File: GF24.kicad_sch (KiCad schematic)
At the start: 65 parts, among them J1 Conn_ARM_SWD_TagConnect_TC2030, J2 USB4110GFA, J3 S2B-PH-SM4-TB, J4 0533980671, J5 0533980671, Q1 3904, Q2 DMN3731U-7, Q3 DMN3731U-7, SW2 BOOT, U1 STM32F031C4T6, U2 SAM-M10Q, U3 TPS745, U4 LTC1733, U5 NE555D, U6 M24C02-WMN6TP, Y1 CS06465-32M

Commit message: updating regulator
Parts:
- removed C14: 0.1uF, MB-Generic:C0603_medium, symbol Device:C
- removed D4: LED, symbol Device:LED
- removed R10: 10k, MB-Generic:R0603_medium, symbol Device:R
- removed R11, R12: 4.7k, MB-Generic:R0603_medium, symbol Device:R
- removed R9: 1k, MB-Generic:R0603_medium, symbol Device:R
- removed U3: TPS745, MB-DFN:6-WDFN, symbol MB-V-REG:TPS74533PQWDRVRQ1
- removed U6: M24C02-WMN6TP, MB-SOIC:SO-8_STM, symbol MB-EEPROM:M24C02-WMN6TP
- added U6: STM32F102C8Tx, Package_QFP:LQFP-48_7x7mm_P0.5mm, symbol MCU_ST_STM32F1:STM32F102C8Tx
- added U7: ~, Package_TO_SOT_SMD:SOT-223-6, symbol MB-V-REG:TPS79533DCQR
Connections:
- net +3V3: now also U7.4 (OUT)
- net REG_I: now also U7.1 (EN)
- net EEPROM-N-WC: no longer names the net of U1.20 (PB2)
- net I2C-SCL: no longer names the net of U1.21 (PB10)
- net I2C-SDA: no longer names the net of U1.22 (PB11)
- new net: U6.23 (VSS), U6.35 (VSS), U6.47 (VSS)
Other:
- note added: "swap for TPS79533DCQR"
- note removed: "EEPROM"
- note removed: "stay under 10mA"
- moved on the sheet: C11, C12, C13, C16, C7, D2, D3, D6, R19, R21, R22, R5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

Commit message: soft complete Rev 2 schematic
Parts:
- removed C1, C2: 4.7uF, MB-Generic:C1206_medium, symbol Device:C
- removed C4: 0.1uF, MB-Generic:C0603_medium, symbol Device:C
- removed C5, C6: 10pF, MB-Generic:C0402_medium, symbol Device:C
- removed J1: Conn_ARM_SWD_TagConnect_TC2030, MB-Conn:Tag-Connect_TC2030-IDC-FP_2x03_P1.27mm_Vertical, symbol Connector:Conn_ARM_SWD_TagConnect_TC2030
- removed J3: S2B-PH-SM4-TB, MB-Conn:JST_S2B-PH-SM4-TB, symbol MB-Conn:S2B-PH-SM4-TB
- removed J4, J5: 0533980671, MB-Conn:MOLEX_0533980671, symbol MB-Conn:0533980671
- removed R1: 10k, MB-Generic:R0603_medium, symbol Device:R
- removed R19, R21, R7, R8: 1k, MB-Generic:R0603_medium, symbol Device:R
- removed R22: 330k, MB-Generic:R0603_medium, symbol Device:R
- removed SW1: ~, MB-SW:PTS815SJM250SMTRLFS, symbol MB-SW:PTS815SJM250SMTRLFS
- removed SW2: BOOT, MB-SW:CJS-1200TA, symbol Switch:SW_Nidec_CAS-120A1
- removed SW3: ~, MB-SW:TL1016AAF160QG, symbol MB-SW:TL1016AAF160QG
- removed U1: STM32F031C4T6, MB-STM:LQFP-48_7x7mm_P0.5mm, symbol MCU_ST_STM32F0:STM32F031C4Tx
- removed U5: NE555D, symbol Timer:NE555D
- removed Y1: CS06465-32M, MB-Crystal:CS06465-32M, symbol Device:Crystal_GND24
- added C10, C12, C13, C15, C19, C8: 100nf, MB-Generic:C1206_medium, symbol Device:C
- added C11, C9: 10uF, MB-Generic:C1206_medium, symbol Device:C
- added C14: 1uF, MB-Generic:C1206_medium, symbol Device:C
- added D1, D4, D8, D9: LED, symbol Device:LED
- added J2: S2B-PH-SM4-TB, MB-Conn:JST_S2B-PH-SM4-TB, symbol MB-Conn:S2B-PH-SM4-TB
- added J3, J6: Conn_01x06_Pin, symbol Connector:Conn_01x06_Pin
- added J4: Conn_ARM_SWD_TagConnect_TC2030, Connector:Tag-Connect_TC2030-IDC-FP_2x03_P1.27mm_Vertical, symbol Connector:Conn_ARM_SWD_TagConnect_TC2030
- added J5: Conn_01x04_Pin, symbol Connector:Conn_01x04_Pin
- added R12: 10k, MB-Generic:R0603_medium, symbol Device:R
- added R2, R3: ~, MB-Generic:R0603_medium, symbol Device:R
- added R4, R5, R6: 1k, MB-Generic:R0603_medium, symbol Device:R
- added S1: 1-1825027-1, MB-SW:SW_1-1825027-1, symbol MB-SW:1-1825027-1
- added SW2: ~, MB-SW:PTS815SJM250SMTRLFS, symbol MB-SW:PTS815SJM250SMTRLFS
- added SW4: BOOT, Button_Switch_SMD:Nidec_Copal_CAS-120A, symbol Switch:SW_Nidec_CAS-120A1
- added TP1, TP2, TP3, TP4, TP5, TP6: TestPoint, symbol Connector:TestPoint
- added X1: ECS-2520MV-160-CN, Oscillator:Oscillator_SMD_ECS_2520MV-xxx-xx-4Pin_2.5x2.0mm, symbol Oscillator:ECS-2520MV-xxx-xx
- C16: value 2.2uF -> 100nf; Distributor Link (none) -> https://www.digikey.com/en/products/detail/kemet/C1206C475K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; Manufacturer (none) -> KEMET; Manufacturer PN (none) -> C1206C475K8RACTU
- C7: value 10nF -> 10uF; footprint MB-Generic:C0402_medium -> MB-Generic:C1206_medium; Distributor Link https://www.digikey.com/en/products/detail/kemet/c0402c103k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 -> https://www.digikey.com/en/products/detail/kemet/C1206C475K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; Manufacturer PN C0402C103K8RACTU -> C1206C475K8RACTU
- Q1: footprint MB-SOT:SOT-23-3 -> Package_TO_SOT_SMD:SOT-323_SC-70
- R8: renamed from R14; value 1k -> was 1k
- R9: renamed from R3; value 1k -> was 1k
- U1: renamed from U7; value ~ -> TPS79533DCQR
- renumbered C9 to C1, C10 to C17, C15 to C18, C8 to C2, C11 to C4, C12 to C5, C13 to C6, D6 to D5, D5 to D6, D1 to D7, J2 to J1, Q3 to Q2, Q2 to Q3, R6 to R1, R4 to R10, R13 to R11, R2 to R13, R15 to R14, R16 to R15, R18 to R16, R5 to R7, SW4 to SW1, SW5 to SW3, U4 to U2, U2 to U3, U6 to U4
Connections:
- net VBUS is gone; now on an unnamed net: C4.1, J1.A4/B9 (VBUS), J1.B4/A9 (VBUS), R1.2, U2.2 (VCC), U2.8 (SEL)
- net +3V3: now also C7.1, U4.1 (VBAT), U4.24 (VDD), U4.36 (VDD), U4.48 (VDD), U4.9 (VDDA), C10.1, C11.1, C12.1, C13.1, C14.1, C15.1, C19.1, C8.1, C9.1, D1.2 (A), D8.2 (A), D9.2 (A), J4.1 (VCC), J5.1 (Pin_1), J6.6 (Pin_6), SW4.1 (C), TP1.1, X1.4 (VDD); no longer C3.1, R8.2, R9.2
- net ACT-H: now also S1.1
- net BAT+: no longer C6.1, U2.9 (BAT)
- net BOOT0_RES: now also R12.1, SW4.2 (B)
- net BUTTON: now also U4.42 (PB6)
- net BUZZER: now also U4.39 (PB3)
- net GND: now also C16.2, Q2.3 (S), Q3.3 (S), U1.3 (GND), U1.6 (GND), U4.23 (VSS), U4.35 (VSS), U4.47 (VSS), U4.8 (VSSA), C10.2, C11.2, C12.2, C13.2, C14.2, C15.2, C19.2, C8.2, C9.2, J2.1, J4.5 (GND), J5.4 (Pin_4), J6.1 (Pin_1), R2.2, S1.2, SW2.2, SW4.3 (A), TP2.1, X1.2 (GND); no longer C16.1, Q2.2 (S), Q3.2 (S)
- net GNSS-3V3: now also D2.2 (A), J3.6 (Pin_6)
- net GNSS-GND: now also J3.1 (Pin_1), R3.2
- net GNSS-N-RESET: now also J3.5 (Pin_5)
- net GNSS-RX: now also J3.4 (Pin_4)
- net GNSS-ST-N-RESET: now also U4.11 (PA1), J6.5 (Pin_5)
- net GNSS-ST-TIMEPULSE: now also U4.14 (PA4), J6.2 (Pin_2)
- net GNSS-TIMEPULSE: now also J3.2 (Pin_2)
- net GNSS-TX: now also J3.3 (Pin_3)
- net MODE: now also U4.43 (PB7)
- net NACPR: now also R4.2; no longer D2.1 (K)
- net NCHRG: now also R6.2; no longer D5.1 (K)
- net NFAULT: now also R5.2; no longer D3.1 (K)
- net NRST: now also C16.1, U4.7 (NRST), J4.3 (~{RESET}), SW2.4
- net REG_I: now also U1.2 (IN)
- net STATG: now also U4.41 (PB5)
- net STATG_QG: now also Q3.2 (G); no longer Q3.1 (G)
- net STATG_QI: now also Q3.1 (D); no longer Q3.3 (D)
- net STATR: now also U4.40 (PB4)
- net STATR_QG: now also Q2.2 (G); no longer Q2.1 (G)
- net STATR_QI: now also Q2.1 (D); no longer Q2.3 (D)
- net SWDCLK: now also U4.37 (PA14), J4.4 (SWCLK)
- net SWDIO: now also U4.34 (PA13), J4.2 (SWDIO)
- net at D3.2 (A): now also D5.2 (A), D4.2 (A), TP5.1
- net at U1.5 (NR): now also C3.1
- net GNSS-ST-TX2: now reaches U4.12 (PA2)
- net GNSS-ST-TX2: now also J6.4 (Pin_4), TP3.1
- net GNSS-ST-RX2: now reaches U4.13 (PA3)
- net GNSS-ST-RX2: now also J6.3 (Pin_3), TP4.1
- net DEBUG_ST_TX: now reaches U4.21 (PB10)
- net DEBUG_ST_TX: now also J5.2 (Pin_2)
- net DEBUG_ST_RX: now reaches U4.22 (PB11)
- net DEBUG_ST_RX: now also J5.3 (Pin_3)
- net BACKUP_DEBUG_ST_TX: now reaches U4.30 (PA9)
- net BACKUP_DEBUG_ST_RX: now reaches U4.31 (PA10)
- net at U4.44 (BOOT0): now also R12.2
- net at U4.5 (PD0): now also X1.3 (OUT)
- new net: D2.1 (K), R3.1
- new net: C6.1, J2.2, TP6.1, U2.9 (BAT)
- new net: D8.1 (K), R8.2
- new net: D3.1 (K), R4.1
- new net: D9.1 (K), R9.2
- new net: D1.1 (K), R2.1
- new net: D5.1 (K), R6.1
- new net: D4.1 (K), R5.1
- no-connect marks 43 -> 42
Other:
- note added: "HSE Bypass"
- note added: "INPUTS/OUTPUTS"
- note added: "No more than 5V should ever be applied to this IC (AMR 7V)"
- note added: "UART Debug"
- note added: "VBAT"
- note added: "external"
- note added: "right angle"
- note removed: "CHARGING"
- note removed: "CONTROLLER"
- note removed: "High Speed External Crystal"
- note removed: "INPUTS"
- note removed: "No more than 5V should ever be applied to this circuit (VBUS-GND)"
- note removed: "OUTPUTS"
- note removed: "PG is open drain when power is not good (lmao). can handle 10mA"
- note removed: "SUBCOMPONENTS"
- note removed: "lmao"
- note removed: "messy :("
- note removed: "swap for TPS79533DCQR"
- note removed: "uC"
- note removed: "uC Power Stability"
- moved on the sheet: BZ1, C1, C17, C18, C2, C4, C5, C6, D5, D6, D7, J1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

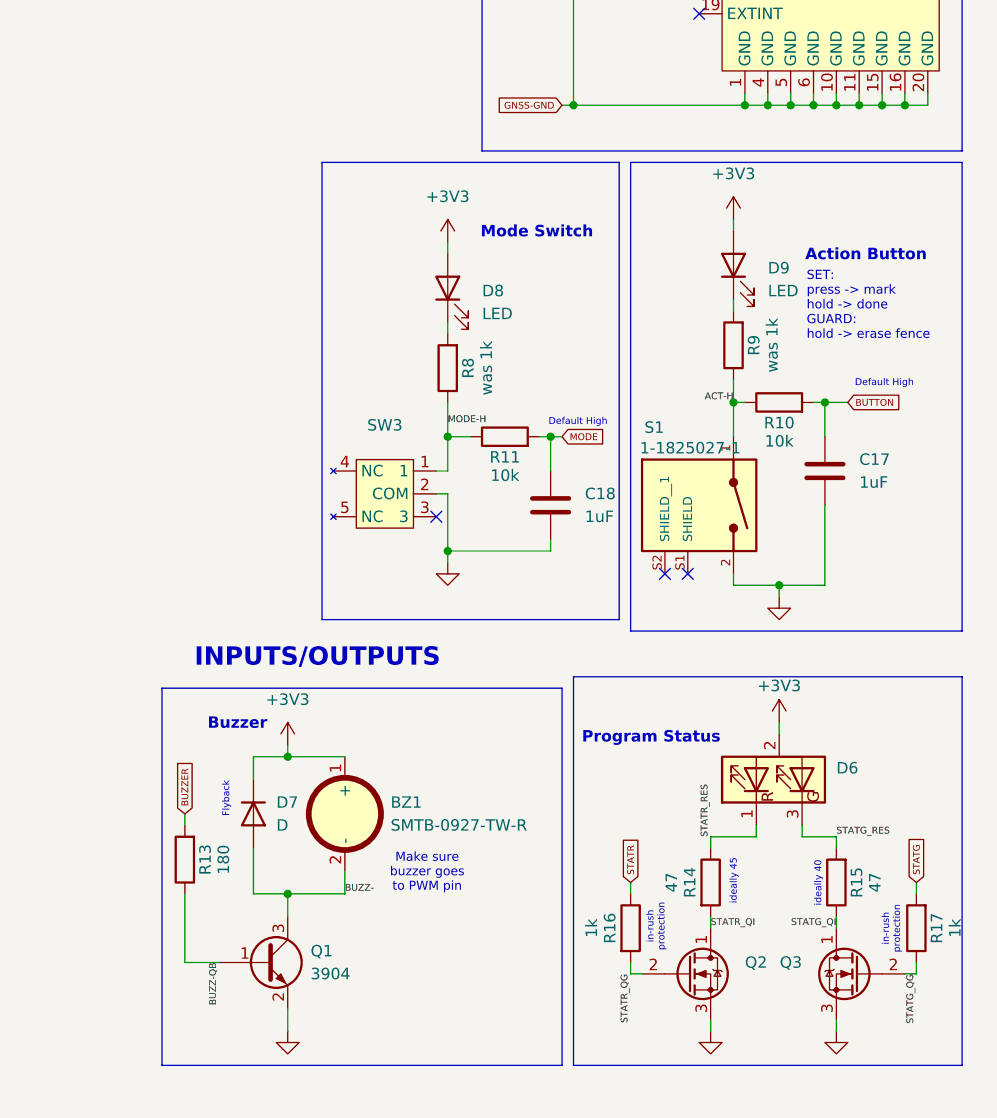
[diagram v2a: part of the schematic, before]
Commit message: changed status LEDs based on testing
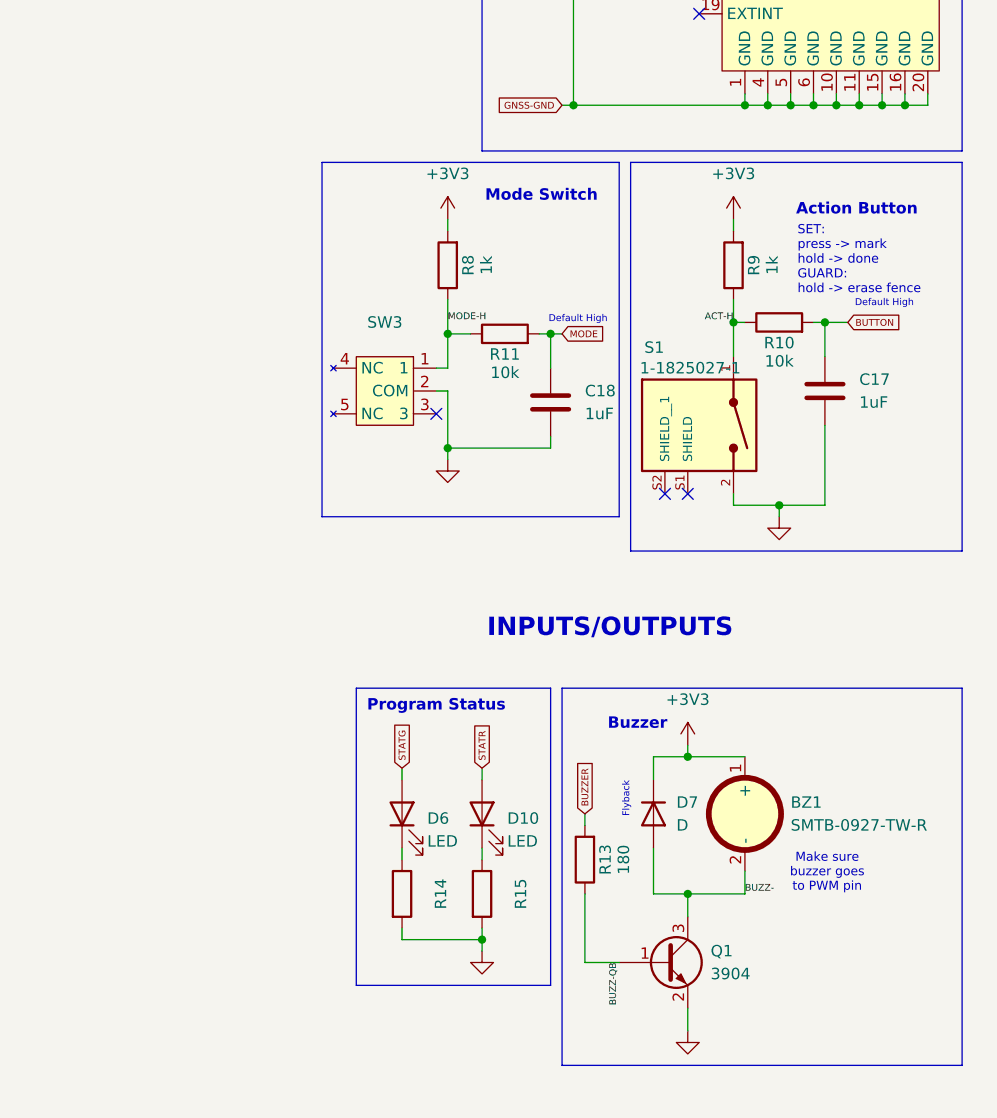
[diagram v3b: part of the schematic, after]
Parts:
- removed D6: APBDA3020SURKCGKC-GX, MB-Opto:Kingbright-APBDA3020, symbol MB-Opto:APBDA3020SURKCGKC-GX
- removed D8, D9: LED, symbol Device:LED
- removed Q2, Q3: DMN3731U-7, MB-SOT:SOT-23-3, symbol Device:Q_NMOS_DGS
- removed R16, R17: 1k, MB-Generic:R0603_medium, symbol Device:R
- added D10, D6: LED, symbol Device:LED
- R14, R15: value 47 -> ~; Distributor Link https://www.digikey.com/en/products/detail/yageo/rc0603fr-0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 -> (none); Manufacturer YAGEO -> (none); Manufacturer PN RC0603FR-0747RL -> (none)
- R8, R9: value was 1k -> 1k
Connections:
- net STATG_RES is gone; now on net GND: R15.2
- net STATR_QI is gone; now on net GND: R14.2
- net +3V3: now also R8.2, R9.2
- net STATG: now also D6.2 (A)
- net STATR: now also D10.2 (A)
- net STATG_QI: no longer names the net of R15.1
- net STATG_QI: now also D10.1 (K)
- net STATR_RES: no longer names the net of R14.1
- net STATR_RES: now also D6.1 (K)
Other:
- note removed: "ideally 40"
- note removed: "ideally 45"
- note removed: "in-rush protection"
- moved on the sheet: BZ1, C17, C18, D7, Q1, R10, R11, R13, R8, R9, S1, SW3
